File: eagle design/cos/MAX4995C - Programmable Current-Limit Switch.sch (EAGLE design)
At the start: 5 parts, among them IC1 MAX4995CAUT+T, J1 61300311121, J2 61300311121

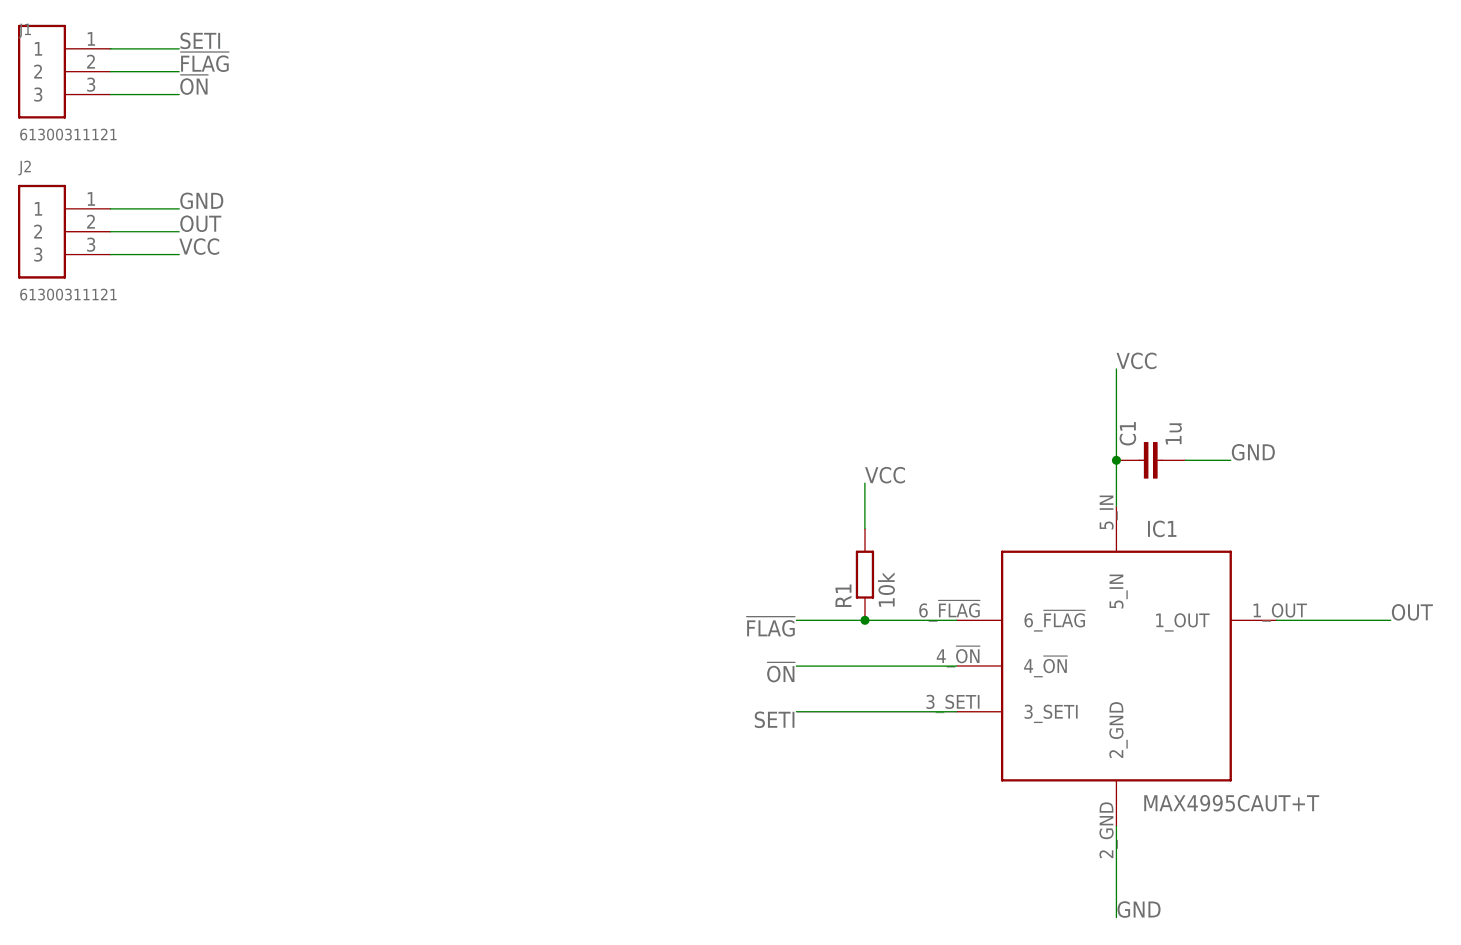
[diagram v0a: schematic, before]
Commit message: HW rev.1 finished routing, created BOM, ERC & DRC check out fine, created gerbers
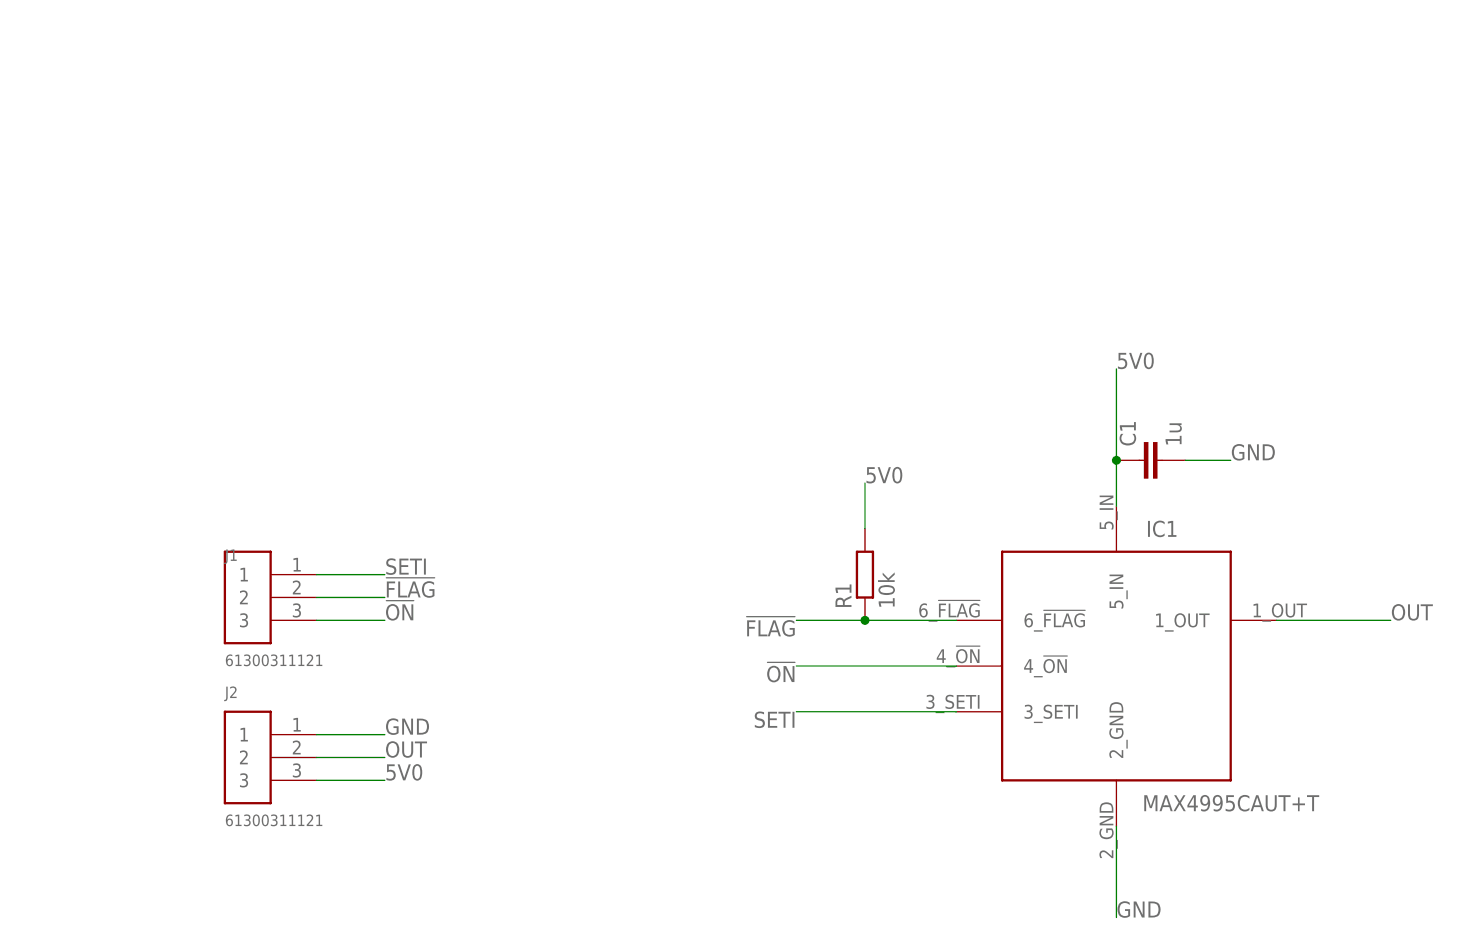
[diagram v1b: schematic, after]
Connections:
- net VCC renamed 5V0
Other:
- moved on the sheet: J1, J2
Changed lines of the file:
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@@
 <attribute name="VALUE" x="60.579" y="62.484" size="1.778" layer="96" rot="R90"/>
 </instance>
-<instance part="J1" gate="G$1" x="-66.04" y="104.14" smashed="yes">
-<attribute name="NAME" x="-68.58" y="108.204" size="1.27" layer="95"/>
-<attribute name="VALUE" x="-68.58" y="96.52" size="1.27" layer="96"/>
+<instance part="J1" gate="G$1" x="-43.18" y="45.72" smashed="yes">
+<attribute name="NAME" x="-45.72" y="49.784" size="1.27" layer="95"/>
+<attribute name="VALUE" x="-45.72" y="38.1" size="1.27" layer="96"/>
 </instance>
-<instance part="J2" gate="G$1" x="-66.04" y="86.36" smashed="yes">
-<attribute name="NAME" x="-68.58" y="92.964" size="1.27" layer="95"/>
-<attribute name="VALUE" x="-68.58" y="78.74" size="1.27" layer="96"/>
+<instance part="J2" gate="G$1" x="-43.18" y="27.94" smashed="yes">
+<attribute name="NAME" x="-45.72" y="34.544" size="1.27" layer="95"/>
+<attribute name="VALUE" x="-45.72" y="20.32" size="1.27" layer="96"/>
 </instance>
 </instances>
@@
 <segment>
 <pinref part="J1" gate="G$1" pin="2"/>
-<wire x1="-58.42" y1="104.14" x2="-50.8" y2="104.14" width="0.1524" layer="91"/>
-<label x="-50.8" y="104.14" size="1.778" layer="95"/>
+<wire x1="-35.56" y1="45.72" x2="-27.94" y2="45.72" width="0.1524" layer="91"/>
+<label x="-27.94" y="45.72" size="1.778" layer="95"/>
 </segment>
 </net>
@@
 <segment>
 <pinref part="J1" gate="G$1" pin="3"/>
-<wire x1="-58.42" y1="101.6" x2="-50.8" y2="101.6" width="0.1524" layer="91"/>
-<label x="-50.8" y="101.6" size="1.778" layer="95"/>
+<wire x1="-35.56" y1="43.18" x2="-27.94" y2="43.18" width="0.1524" layer="91"/>
+<label x="-27.94" y="43.18" size="1.778" layer="95"/>
 </segment>
 </net>
@@
 <segment>
 <pinref part="J2" gate="G$1" pin="1"/>
-<wire x1="-58.42" y1="88.9" x2="-50.8" y2="88.9" width="0.1524" layer="91"/>
-<label x="-50.8" y="88.9" size="1.778" layer="95"/>
+<wire x1="-35.56" y1="30.48" x2="-27.94" y2="30.48" width="0.1524" layer="91"/>
+<label x="-27.94" y="30.48" size="1.778" layer="95"/>
 </segment>
 </net>
@@
 <segment>
 <pinref part="J2" gate="G$1" pin="2"/>
-<wire x1="-58.42" y1="86.36" x2="-50.8" y2="86.36" width="0.1524" layer="91"/>
-<label x="-50.8" y="86.36" size="1.778" layer="95"/>
+<wire x1="-35.56" y1="27.94" x2="-27.94" y2="27.94" width="0.1524" layer="91"/>
+<label x="-27.94" y="27.94" size="1.778" layer="95"/>
 </segment>
 </net>
-<net name="VCC" class="1">
+<net name="5V0" class="1">
 <segment>
 <pinref part="IC1" gate="G$1" pin="5_IN"/>
@@
 <segment>
 <pinref part="J2" gate="G$1" pin="3"/>
-<wire x1="-58.42" y1="83.82" x2="-50.8" y2="83.82" width="0.1524" layer="91"/>
-<label x="-50.8" y="83.82" size="1.778" layer="95"/>
+<wire x1="-35.56" y1="25.4" x2="-27.94" y2="25.4" width="0.1524" layer="91"/>
+<label x="-27.94" y="25.4" size="1.778" layer="95"/>
 </segment>
 </net>
@@
 <segment>
 <pinref part="J1" gate="G$1" pin="1"/>
-<wire x1="-58.42" y1="106.68" x2="-50.8" y2="106.68" width="0.1524" layer="91"/>
-<label x="-50.8" y="106.68" size="1.778" layer="95"/>
+<wire x1="-35.56" y1="48.26" x2="-27.94" y2="48.26" width="0.1524" layer="91"/>
+<label x="-27.94" y="48.26" size="1.778" layer="95"/>
 </segment>
 <segment>
